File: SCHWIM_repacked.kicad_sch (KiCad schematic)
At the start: 7 parts, among them J1 SWIM Connector, U1 74HCT244, U2 74HCT32

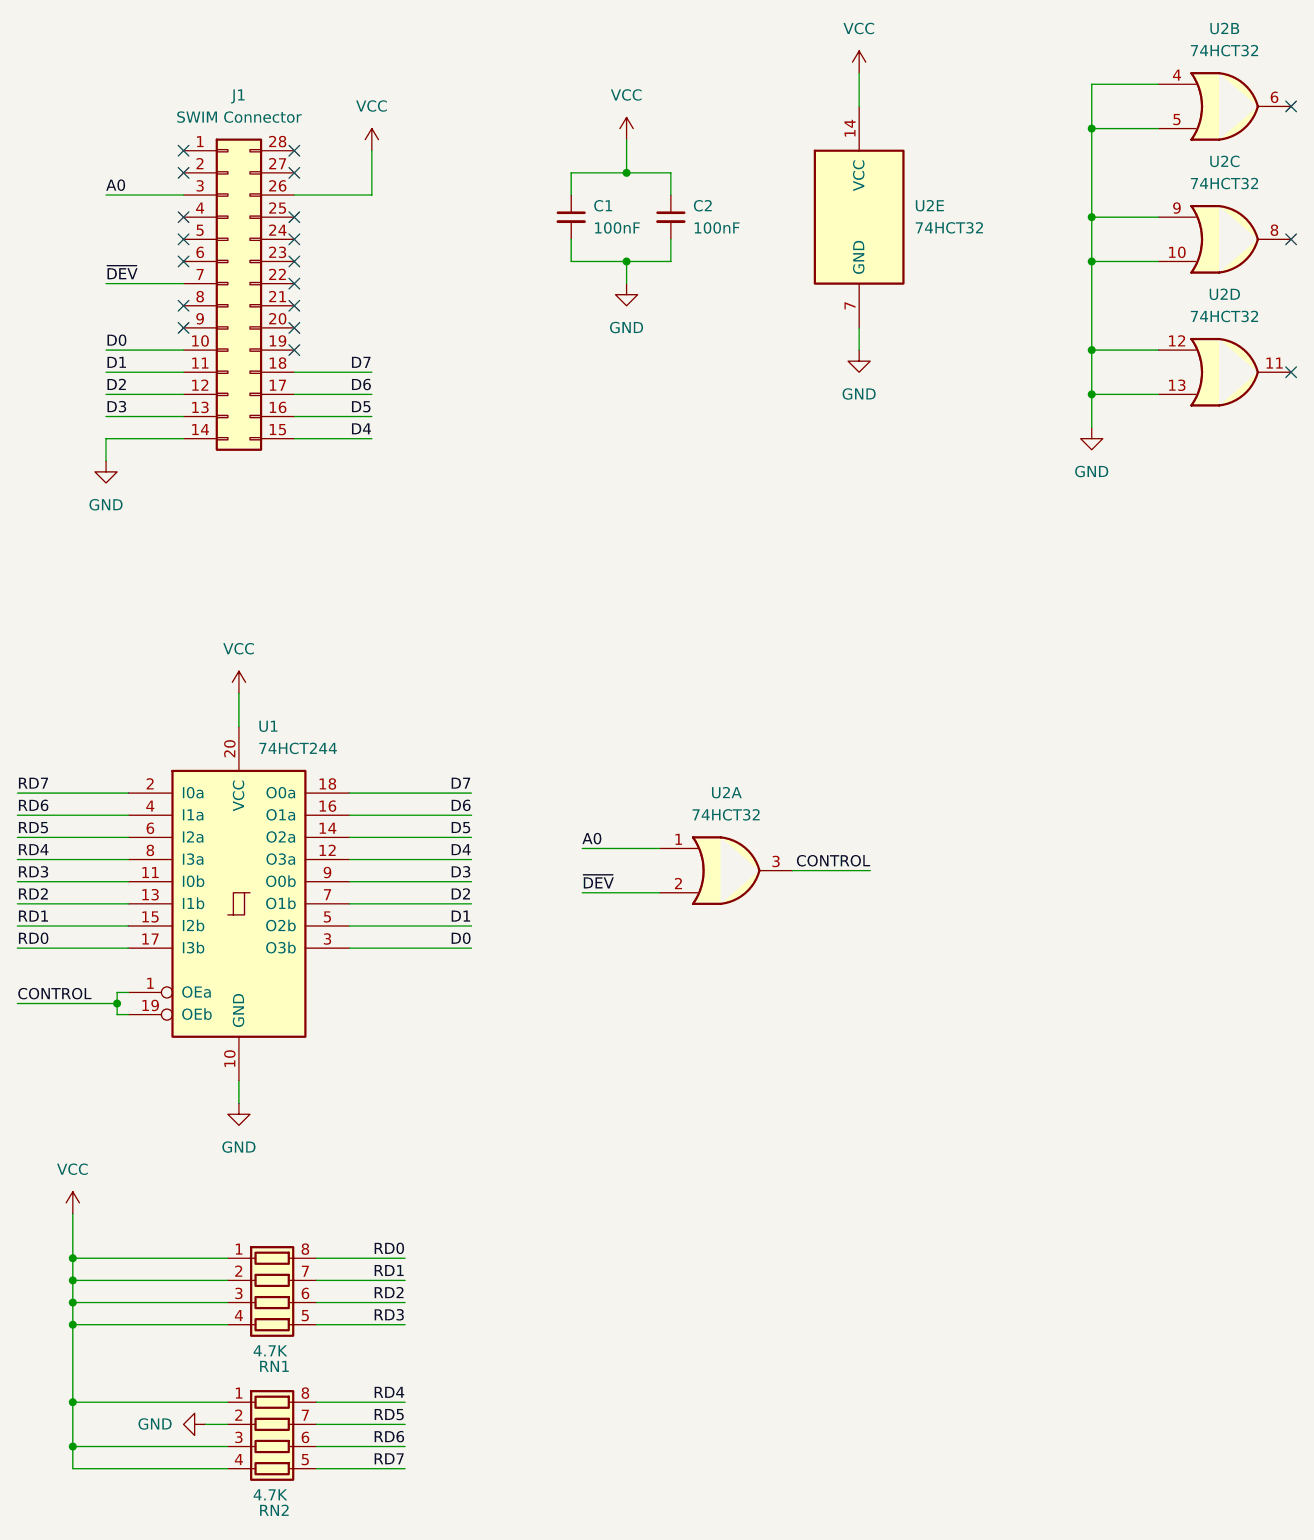
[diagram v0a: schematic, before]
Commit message: Use a single or gate
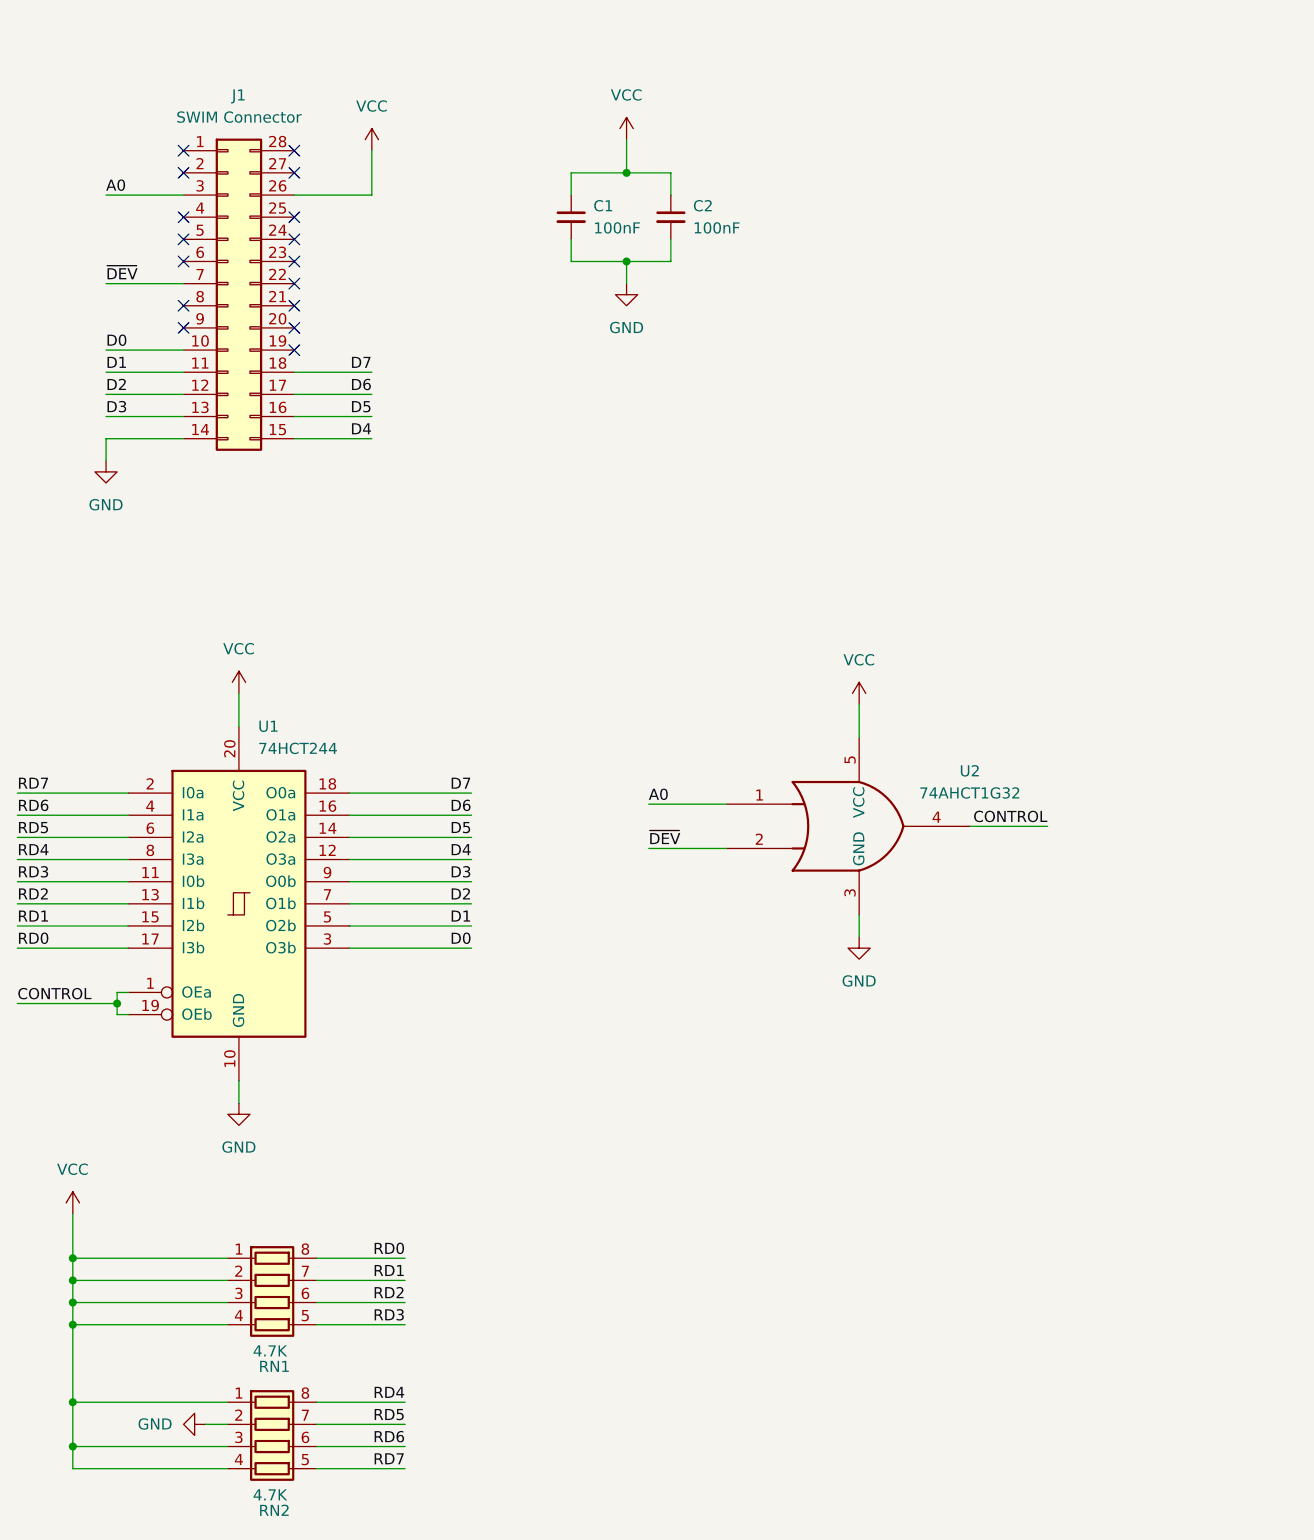
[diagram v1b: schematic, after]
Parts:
- removed U2: 74HCT32, Package_SO:TSSOP-14_4.4x5mm_P0.65mm, symbol 74xx:74LS32
- added U2: 74AHCT1G32, Package_TO_SOT_SMD:SOT-353_SC-70-5_Handsoldering, symbol 74xGxx:74AHCT1G32
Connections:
- net A0: now also U2.1
- net CONTROL: now also U2.4
- net GND: now also U2.3 (GND)
- net VCC: now also U2.5 (VCC)
- net ~{DEV}: now also U2.2
- no-connect marks 19 -> 16

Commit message: Added rev.1 of the repacked schwim, fixed footprint for U2
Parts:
- U2: footprint Package_TO_SOT_SMD:SOT-353_SC-70-5_Handsoldering -> Package_TO_SOT_SMD:SOT-23-5_HandSoldering
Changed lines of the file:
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@@
 (kicad_sch
-	(version 20231120)
+	(version 20250114)
 	(generator "eeschema")
-	(generator_version "8.0")
+	(generator_version "9.0")
 	(paper "A4")
 	(junction
@@
 	(label "D7"
 		(at 62.23 60.96 180)
-		(fields_autoplaced yes)
 		(effects
 			(font
@@
 	(label "CONTROL"
 		(at 21.59 133.35 0)
-		(fields_autoplaced yes)
 		(effects
 			(font
@@
 	(label "D6"
 		(at 73.66 111.76 180)
-		(fields_autoplaced yes)
 		(effects
 			(font
@@
 	(label "A0"
 		(at 93.98 110.49 0)
-		(fields_autoplaced yes)
 		(effects
 			(font
@@
 	(label "RD7"
 		(at 21.59 109.22 0)
-		(fields_autoplaced yes)
 		(effects
 			(font
@@
 	(label "RD5"
 		(at 66.04 181.61 180)
-		(fields_autoplaced yes)
 		(effects
 			(font
@@
 	(label "D5"
 		(at 73.66 114.3 180)
-		(fields_autoplaced yes)
 		(effects
 			(font
@@
 	(label "~{DEV}"
 		(at 31.75 50.8 0)
-		(fields_autoplaced yes)
 		(effects
 			(font
@@
 	(label "RD0"
 		(at 66.04 162.56 180)
-		(fields_autoplaced yes)
 		(effects
 			(font
@@
 	(label "D1"
 		(at 73.66 124.46 180)
-		(fields_autoplaced yes)
 		(effects
 			(font
@@
 	(label "RD6"
 		(at 66.04 184.15 180)
-		(fields_autoplaced yes)
 		(effects
 			(font
@@
 	(label "RD1"
 		(at 66.04 165.1 180)
-		(fields_autoplaced yes)
 		(effects
 			(font
@@
 	(label "~{DEV}"
 		(at 93.98 115.57 0)
-		(fields_autoplaced yes)
 		(effects
 			(font
@@
 	(label "D3"
 		(at 31.75 66.04 0)
-		(fields_autoplaced yes)
 		(effects
 			(font
@@
 	(label "RD7"
 		(at 66.04 186.69 180)
-		(fields_autoplaced yes)
 		(effects
 			(font
@@
 	(label "RD5"
 		(at 21.59 114.3 0)
-		(fields_autoplaced yes)
 		(effects
 			(font
@@
 	(label "RD0"
 		(at 21.59 127 0)
-		(fields_autoplaced yes)
 		(effects
 			(font
@@
 	(label "D3"
 		(at 73.66 119.38 180)
-		(fields_autoplaced yes)
 		(effects
 			(font
@@
 	(label "D1"
 		(at 31.75 60.96 0)
-		(fields_autoplaced yes)
 		(effects
 			(font
@@
 	(label "RD3"
 		(at 21.59 119.38 0)
-		(fields_autoplaced yes)
 		(effects
 			(font
@@
 	(label "D2"
 		(at 31.75 63.5 0)
-		(fields_autoplaced yes)
 		(effects
 			(font
@@
 	(label "RD2"
 		(at 66.04 167.64 180)
-		(fields_autoplaced yes)
 		(effects
 			(font
@@
 	(label "RD4"
 		(at 21.59 116.84 0)
-		(fields_autoplaced yes)
 		(effects
 			(font
@@
 	(label "D5"
 		(at 62.23 66.04 180)
-		(fields_autoplaced yes)
 		(effects
 			(font
@@
 	(label "CONTROL"
 		(at 139.7 113.03 180)
-		(fields_autoplaced yes)
 		(effects
 			(font
@@
 	(label "D4"
 		(at 62.23 68.58 180)
-		(fields_autoplaced yes)
 		(effects
 			(font
@@
 	(label "D0"
 		(at 31.75 58.42 0)
-		(fields_autoplaced yes)
 		(effects
 			(font
@@
 	(label "RD1"
 		(at 21.59 124.46 0)
-		(fields_autoplaced yes)
 		(effects
 			(font
@@
 	(label "RD6"
 		(at 21.59 111.76 0)
-		(fields_autoplaced yes)
 		(effects
 			(font
@@
 	(label "RD2"
 		(at 21.59 121.92 0)
-		(fields_autoplaced yes)
 		(effects
 			(font
@@
 	(label "A0"
 		(at 31.75 40.64 0)
-		(fields_autoplaced yes)
 		(effects
 			(font
@@
 	(label "RD3"
 		(at 66.04 170.18 180)
-		(fields_autoplaced yes)
 		(effects
 			(font
@@
 	(label "D0"
 		(at 73.66 127 180)
-		(fields_autoplaced yes)
 		(effects
 			(font
@@
 	(label "RD4"
 		(at 66.04 179.07 180)
-		(fields_autoplaced yes)
 		(effects
 			(font
@@
 	(label "D7"
 		(at 73.66 109.22 180)
-		(fields_autoplaced yes)
 		(effects
 			(font
@@
 	(label "D2"
 		(at 73.66 121.92 180)
-		(fields_autoplaced yes)
 		(effects
 			(font
@@
 	(label "D6"
 		(at 62.23 63.5 180)
-		(fields_autoplaced yes)
 		(effects
 			(font
@@
 	(label "D4"
 		(at 73.66 116.84 180)
-		(fields_autoplaced yes)
 		(effects
 			(font
@@
 			)
 		)
-		(property "Footprint" "Package_TO_SOT_SMD:SOT-353_SC-70-5_Handsoldering"
+		(property "Footprint" "Package_TO_SOT_SMD:SOT-23-5_HandSoldering"
 			(at 118.11 113.03 0)
 			(effects
@@
 		)
 	)
+	(embedded_fonts no)
 )
